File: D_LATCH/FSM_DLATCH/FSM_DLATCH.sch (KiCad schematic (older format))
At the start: 13 parts, among them U1 4050

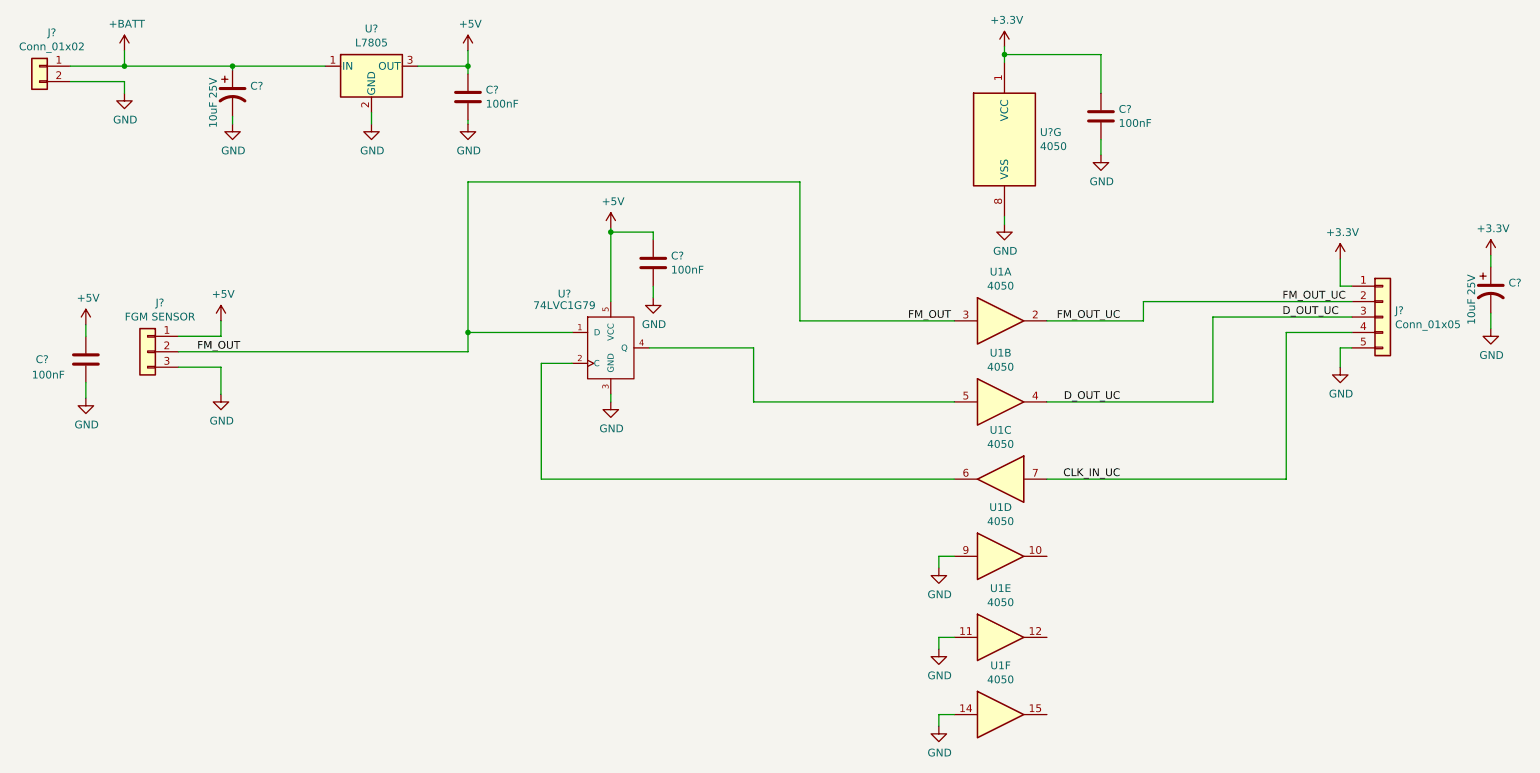
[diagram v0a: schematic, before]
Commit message: D_Latch design is finish
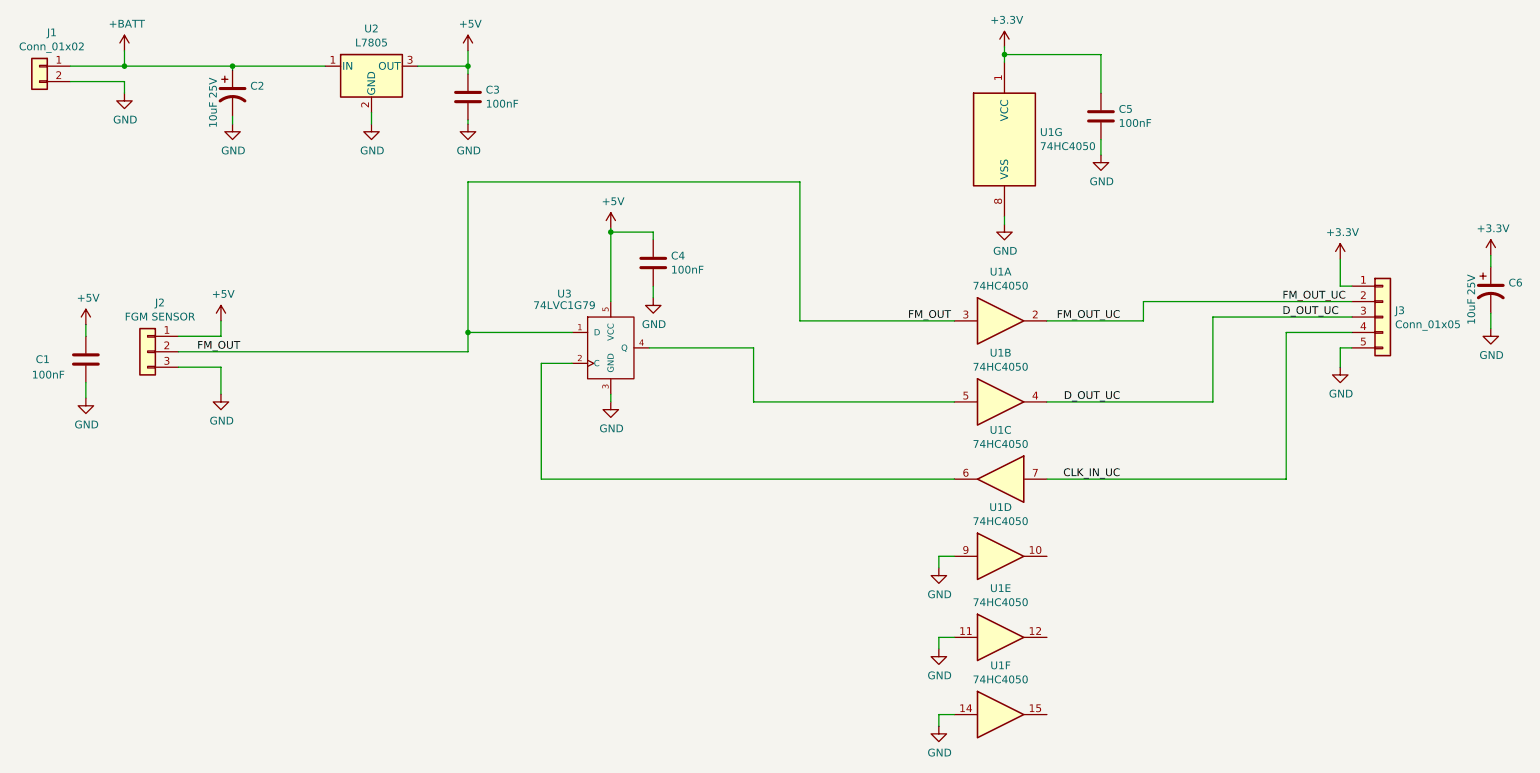
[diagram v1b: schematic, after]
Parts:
- C1, C3, C4, C5: renamed from C?; footprint (none) -> Capacitors_SMD:C_1206
- C2, C6: renamed from C?; footprint (none) -> Capacitors_THT:CP_Radial_D5.0mm_P2.50mm
- J1: renamed from J?; footprint (none) -> Connectors_Terminal_Blocks:TerminalBlock_bornier-2_P5.08mm
- J2: renamed from J?; footprint (none) -> Connectors_Samtec:SL-103-X-XX_1x03
- J3: renamed from J?; footprint (none) -> Connectors_Samtec:SL-105-X-XX_1x05
- U1: value 4050 -> 74HC4050; footprint (none) -> Housings_SOIC:SOIC-16_3.9x9.9mm_Pitch1.27mm; SUPPLIER (none) -> 1085272
- U1: value 4050 -> 74HC4050; footprint (none) -> Housings_SOIC:SOIC-16_3.9x9.9mm_Pitch1.27mm
- U1: renamed from U?; value 4050 -> 74HC4050; footprint (none) -> Housings_SOIC:SOIC-16_3.9x9.9mm_Pitch1.27mm
- U2: renamed from U?; footprint (none) -> TO_SOT_Packages_SMD:TO-252-2
- U3: renamed from U?; footprint (none) -> TO_SOT_Packages_SMD:SOT-23-5_HandSoldering; SUPPLIER (none) -> F:2342442
